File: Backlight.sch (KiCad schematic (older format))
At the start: 26 parts, among them U201 TPS61181, U202 TPS61181

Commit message: Initial footprint association, last few footprints
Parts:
- C201, C202, C203, C204, C207, C208: footprint (none) -> FT:1206
- C205, C206: footprint (none) -> SMD_Packages:SMD-0402_c
- D201, D202: footprint (none) -> novepad:POWERDI123_DIODE
- L201, L202: footprint (none) -> novepad:NR4018_IND
- R201, R202, R203, R204, R205: footprint (none) -> FT:0603
- TP201, TP202, TP203, TP204, TP205, TP206: footprint (none) -> novepad:SMD_TEST_POINT
- U201, U202: footprint (none) -> novepad:QFN50P300X300X80-17N
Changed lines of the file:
@@
 LIBS:valves
 LIBS:novepad-cache
-EELAYER 24 0
+EELAYER 25 0
 EELAYER END
 $Descr A4 11693 8268
@@
 F 0 "R201" V 1430 2200 40  0000 C CNN
 F 1 "0R DNP" V 1357 2201 40  0000 C CNN
-F 2 "" V 1280 2200 30  0000 C CNN
+F 2 "FT:0603" V 1280 2200 30  0001 C CNN
 F 3 "" H 1350 2200 30  0000 C CNN
 	1    1350 2200
@@
 F 0 "TP202" H 1880 1400 40  0000 L CNN
 F 1 "CONN_1" H 1800 1455 30  0001 C CNN
-F 2 "" H 1800 1400 60  0000 C CNN
+F 2 "novepad:SMD_TEST_POINT" H 1800 1400 60  0001 C CNN
 F 3 "" H 1800 1400 60  0000 C CNN
 	1    1800 1400
@@
 F 0 "TP203" H 1880 1550 40  0000 L CNN
 F 1 "CONN_1" H 1800 1605 30  0001 C CNN
-F 2 "" H 1800 1550 60  0000 C CNN
+F 2 "novepad:SMD_TEST_POINT" H 1800 1550 60  0001 C CNN
 F 3 "" H 1800 1550 60  0000 C CNN
 	1    1800 1550
@@
 F 0 "TP201" H 1730 2050 40  0000 L CNN
 F 1 "CONN_1" H 1650 2105 30  0001 C CNN
-F 2 "" H 1650 2050 60  0000 C CNN
+F 2 "novepad:SMD_TEST_POINT" H 1650 2050 60  0001 C CNN
 F 3 "" H 1650 2050 60  0000 C CNN
 	1    1650 2050
@@
 F 0 "TP204" H 2830 1000 40  0000 L CNN
 F 1 "CONN_1" H 2750 1055 30  0001 C CNN
-F 2 "" H 2750 1000 60  0000 C CNN
+F 2 "novepad:SMD_TEST_POINT" H 2750 1000 60  0001 C CNN
 F 3 "" H 2750 1000 60  0000 C CNN
 	1    2750 1000
@@
 F 0 "U202" H 5650 5000 60  0000 C CNN
 F 1 "TPS61181" H 5100 5600 60  0000 C CNN
-F 2 "" H 5550 5600 60  0000 C CNN
+F 2 "novepad:QFN50P300X300X80-17N" H 5550 5600 60  0001 C CNN
 F 3 "" H 5550 5600 60  0000 C CNN
 	1    5100 5550
@@
 F 0 "C203" H 3300 4750 40  0000 L CNN
 F 1 "4.7uF 25V" H 3306 4565 40  0000 L CNN
-F 2 "" H 3338 4500 30  0000 C CNN
+F 2 "FT:1206" H 3338 4500 30  0001 C CNN
 F 3 "" H 3300 4650 60  0000 C CNN
 	1    3300 4650
@@
 F 0 "R203" V 3830 4700 40  0000 C CNN
 F 1 "51R" V 3757 4701 40  0000 C CNN
-F 2 "" V 3680 4700 30  0000 C CNN
+F 2 "FT:0603" V 3680 4700 30  0001 C CNN
 F 3 "" H 3750 4700 30  0000 C CNN
 	1    3750 4700
@@
 F 0 "C204" H 3300 5500 40  0000 L CNN
 F 1 "1uF 25V" H 3306 5315 40  0000 L CNN
-F 2 "" H 3338 5250 30  0000 C CNN
+F 2 "FT:1206" H 3338 5250 30  0001 C CNN
 F 3 "" H 3300 5400 60  0000 C CNN
 	1    3300 5400
@@
 F 0 "C206" H 3650 5900 40  0000 L CNN
 F 1 "100nF" H 3656 5715 40  0000 L CNN
-F 2 "" H 3688 5650 30  0000 C CNN
+F 2 "SMD_Packages:SMD-0402_c" H 3688 5650 30  0001 C CNN
 F 3 "" H 3650 5800 60  0000 C CNN
 	1    3650 5800
@@
 F 0 "R205" V 4080 6300 40  0000 C CNN
 F 1 "68K 1%" V 4007 6301 40  0000 C CNN
-F 2 "" V 3930 6300 30  0000 C CNN
+F 2 "FT:0603" V 3930 6300 30  0001 C CNN
 F 3 "" H 4000 6300 30  0000 C CNN
 	1    4000 6300
@@
 F 0 "L202" H 4800 4550 40  0000 C CNN
 F 1 "10uH NR4018T100M" H 4850 4350 40  0000 C CNN
-F 2 "" H 4900 4450 60  0000 C CNN
+F 2 "novepad:NR4018_IND" H 4900 4450 60  0001 C CNN
 F 3 "" H 4900 4450 60  0000 C CNN
 	1    4900 4450
@@
 F 0 "TP206" H 4630 4750 40  0000 L CNN
 F 1 "CONN_1" H 4550 4805 30  0001 C CNN
-F 2 "" H 4550 4750 60  0000 C CNN
+F 2 "novepad:SMD_TEST_POINT" H 4550 4750 60  0001 C CNN
 F 3 "" H 4550 4750 60  0000 C CNN
 	1    4550 4750
@@
 F 0 "D202" H 5750 4550 40  0000 C CNN
 F 1 "DFLS160-7" H 5750 4350 40  0000 C CNN
-F 2 "" H 5750 4450 60  0000 C CNN
+F 2 "novepad:POWERDI123_DIODE" H 5750 4450 60  0001 C CNN
 F 3 "" H 5750 4450 60  0000 C CNN
 	1    5750 4450
@@
 F 0 "C208" H 6050 4800 40  0000 L CNN
 F 1 "4.7uF 25V" H 6056 4615 40  0000 L CNN
-F 2 "" H 6088 4550 30  0000 C CNN
+F 2 "FT:1206" H 6088 4550 30  0001 C CNN
 F 3 "" H 6050 4700 60  0000 C CNN
 	1    6050 4700
@@
 F 0 "U201" H 5650 2300 60  0000 C CNN
 F 1 "TPS61181" H 5100 2900 60  0000 C CNN
-F 2 "" H 5550 2900 60  0000 C CNN
+F 2 "novepad:QFN50P300X300X80-17N" H 5550 2900 60  0001 C CNN
 F 3 "" H 5550 2900 60  0000 C CNN
 	1    5100 2850
@@
 F 0 "C201" H 3300 2050 40  0000 L CNN
 F 1 "4.7uF 25V" H 3306 1865 40  0000 L CNN
-F 2 "" H 3338 1800 30  0000 C CNN
+F 2 "FT:1206" H 3338 1800 30  0001 C CNN
 F 3 "" H 3300 1950 60  0000 C CNN
 	1    3300 1950
@@
 F 0 "R202" V 3830 2000 40  0000 C CNN
 F 1 "51R" V 3757 2001 40  0000 C CNN
-F 2 "" V 3680 2000 30  0000 C CNN
+F 2 "FT:0603" V 3680 2000 30  0001 C CNN
 F 3 "" H 3750 2000 30  0000 C CNN
 	1    3750 2000
@@
 F 0 "C202" H 3300 2800 40  0000 L CNN
 F 1 "1uF 25V" H 3306 2615 40  0000 L CNN
-F 2 "" H 3338 2550 30  0000 C CNN
+F 2 "FT:1206" H 3338 2550 30  0001 C CNN
 F 3 "" H 3300 2700 60  0000 C CNN
 	1    3300 2700
@@
 F 0 "C205" H 3650 3200 40  0000 L CNN
 F 1 "100nF" H 3656 3015 40  0000 L CNN
-F 2 "" H 3688 2950 30  0000 C CNN
+F 2 "SMD_Packages:SMD-0402_c" H 3688 2950 30  0001 C CNN
 F 3 "" H 3650 3100 60  0000 C CNN
 	1    3650 3100
@@
 F 0 "R204" V 4080 3600 40  0000 C CNN
 F 1 "68K 1%" V 4007 3601 40  0000 C CNN
-F 2 "" V 3930 3600 30  0000 C CNN
+F 2 "FT:0603" V 3930 3600 30  0001 C CNN
 F 3 "" H 4000 3600 30  0000 C CNN
 	1    4000 3600
@@
 F 0 "L201" H 4800 1850 40  0000 C CNN
 F 1 "10uH NR4018T100M" H 4850 1650 40  0000 C CNN
-F 2 "" H 4900 1750 60  0000 C CNN
+F 2 "novepad:NR4018_IND" H 4900 1750 60  0001 C CNN
 F 3 "" H 4900 1750 60  0000 C CNN
 	1    4900 1750
@@
 F 0 "TP205" H 4630 2050 40  0000 L CNN
 F 1 "CONN_1" H 4550 2105 30  0001 C CNN
-F 2 "" H 4550 2050 60  0000 C CNN
+F 2 "novepad:SMD_TEST_POINT" H 4550 2050 60  0001 C CNN
 F 3 "" H 4550 2050 60  0000 C CNN
 	1    4550 2050
@@
 F 0 "D201" H 5750 1850 40  0000 C CNN
 F 1 "DFLS160-7" H 5750 1650 40  0000 C CNN
-F 2 "" H 5750 1750 60  0000 C CNN
+F 2 "novepad:POWERDI123_DIODE" H 5750 1750 60  0001 C CNN
 F 3 "" H 5750 1750 60  0000 C CNN
 	1    5750 1750
@@
 F 0 "C207" H 6050 2100 40  0000 L CNN
 F 1 "4.7uF 25V" H 6056 1915 40  0000 L CNN
-F 2 "" H 6088 1850 30  0000 C CNN
+F 2 "FT:1206" H 6088 1850 30  0001 C CNN
 F 3 "" H 6050 2000 60  0000 C CNN
 	1    6050 2000
@@
 F 0 "TH201" V 1710 890 50  0000 C CNN
 F 1 "NTPA7220LBMB0 1A 22R INRUSH LIMITER" V 1930 1000 50  0000 C CNN
-F 2 "" H 1800 1000 60  0000 C CNN
+F 2 "" H 1800 1000 60  0001 C CNN
 F 3 "" H 1800 1000 60  0000 C CNN
 	1    1800 1000

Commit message: First attempt at routing the high speed differential traces
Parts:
- TH201: footprint (none) -> novepad:PTH_2HOLE_5MM
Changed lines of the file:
@@
 F 0 "TH201" V 1710 890 50  0000 C CNN
 F 1 "NTPA7220LBMB0 1A 22R INRUSH LIMITER" V 1930 1000 50  0000 C CNN
-F 2 "" H 1800 1000 60  0001 C CNN
+F 2 "novepad:PTH_2HOLE_5MM" H 1800 1000 60  0001 C CNN
 F 3 "" H 1800 1000 60  0000 C CNN
 	1    1800 1000

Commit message: Super-zealous length matching version
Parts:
- C205, C206: footprint SMD_Packages:SMD-0402_c -> FT:C0402
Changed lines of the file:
@@
 F 0 "C206" H 3650 5900 40  0000 L CNN
 F 1 "100nF" H 3656 5715 40  0000 L CNN
-F 2 "SMD_Packages:SMD-0402_c" H 3688 5650 30  0001 C CNN
+F 2 "FT:C0402" H 3688 5650 30  0001 C CNN
 F 3 "" H 3650 5800 60  0000 C CNN
 	1    3650 5800
@@
 F 0 "C205" H 3650 3200 40  0000 L CNN
 F 1 "100nF" H 3656 3015 40  0000 L CNN
-F 2 "SMD_Packages:SMD-0402_c" H 3688 2950 30  0001 C CNN
+F 2 "FT:C0402" H 3688 2950 30  0001 C CNN
 F 3 "" H 3650 3100 60  0000 C CNN
 	1    3650 3100

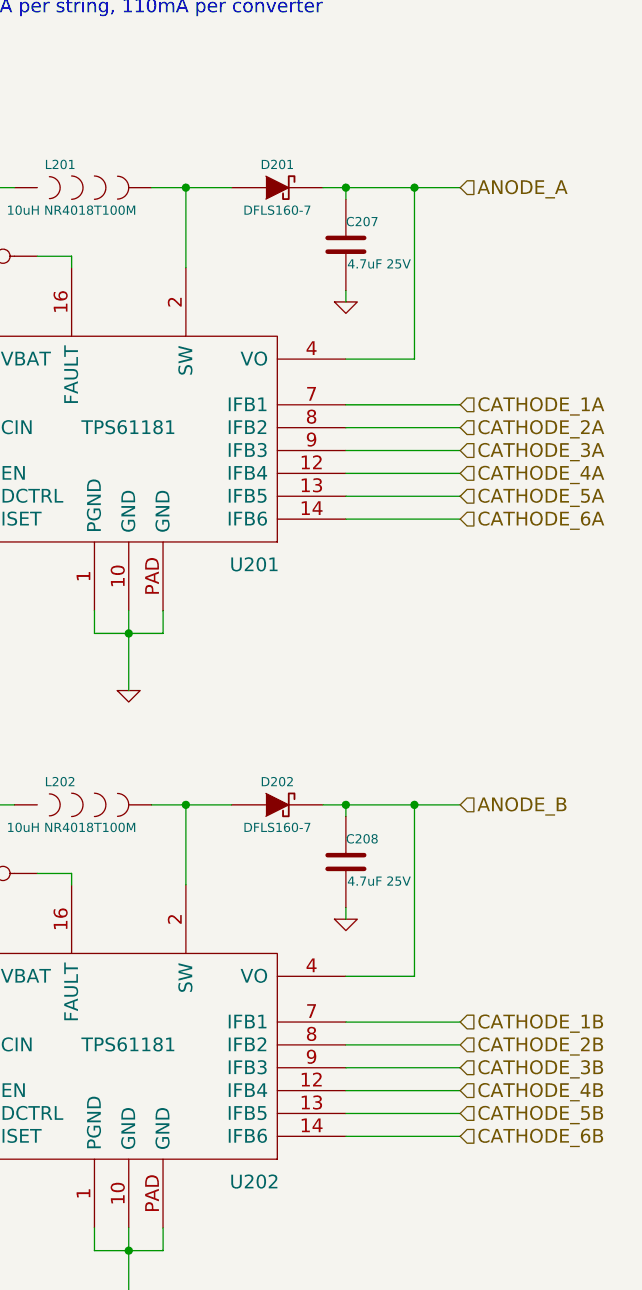
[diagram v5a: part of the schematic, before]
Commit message: Routed, passes DRC
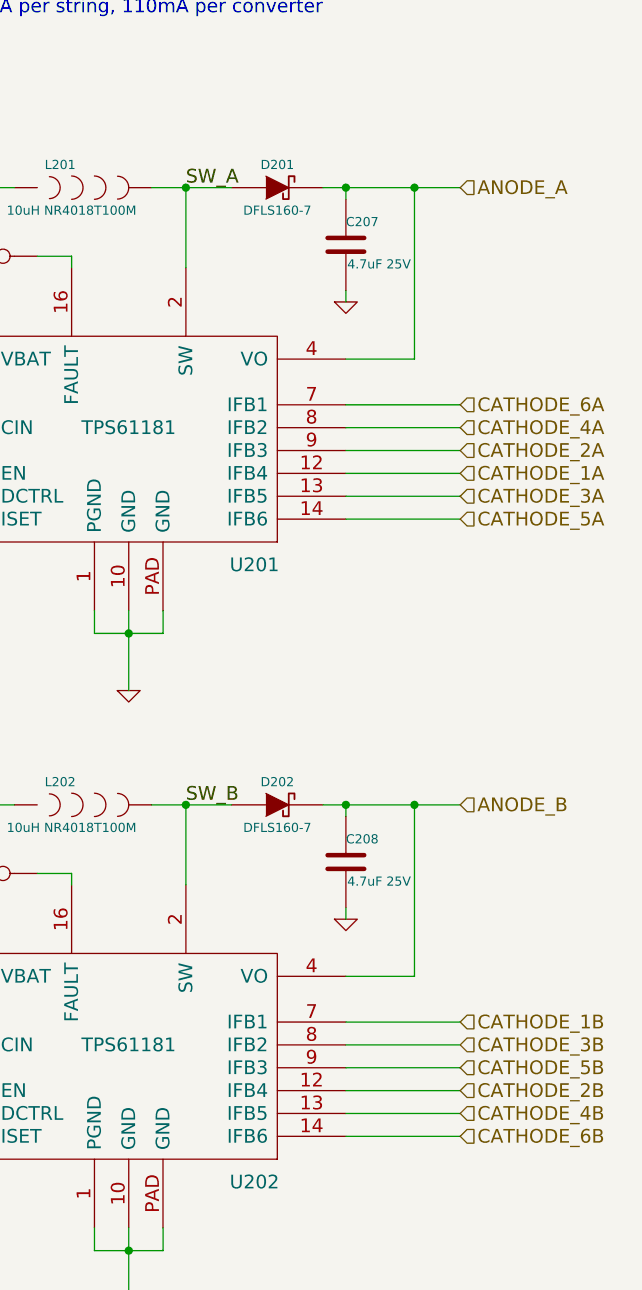
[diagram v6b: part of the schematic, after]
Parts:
- C201, C203, C207, C208: footprint FT:1206 -> FT:0805
- C202, C204: footprint FT:1206 -> FT:0603
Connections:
- net labels added: SW_A, SW_B
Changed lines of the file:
@@
 Text HLabel 6550 1750 2    60   Input ~ 0
 ANODE_A
+Text HLabel 6550 3000 2    60   Input ~ 0
+CATHODE_1A
+Text HLabel 6550 2900 2    60   Input ~ 0
+CATHODE_2A
+Text HLabel 6550 3100 2    60   Input ~ 0
+CATHODE_3A
+Text HLabel 6550 2800 2    60   Input ~ 0
+CATHODE_4A
+Text HLabel 6550 3200 2    60   Input ~ 0
+CATHODE_5A
 Text HLabel 6550 2700 2    60   Input ~ 0
-CATHODE_1A
-Text HLabel 6550 2800 2    60   Input ~ 0
-CATHODE_2A
-Text HLabel 6550 2900 2    60   Input ~ 0
-CATHODE_3A
-Text HLabel 6550 3000 2    60   Input ~ 0
-CATHODE_4A
-Text HLabel 6550 3100 2    60   Input ~ 0
-CATHODE_5A
-Text HLabel 6550 3200 2    60   Input ~ 0
 CATHODE_6A
 Text HLabel 6550 4450 2    60   Input ~ 0
@@
 Text HLabel 6550 5400 2    60   Input ~ 0
 CATHODE_1B
+Text HLabel 6550 5700 2    60   Input ~ 0
+CATHODE_2B
 Text HLabel 6550 5500 2    60   Input ~ 0
-CATHODE_2B
+CATHODE_3B
+Text HLabel 6550 5800 2    60   Input ~ 0
+CATHODE_4B
 Text HLabel 6550 5600 2    60   Input ~ 0
-CATHODE_3B
-Text HLabel 6550 5700 2    60   Input ~ 0
-CATHODE_4B
-Text HLabel 6550 5800 2    60   Input ~ 0
 CATHODE_5B
 Text HLabel 6550 5900 2    60   Input ~ 0
@@
 F 0 "C203" H 3300 4750 40  0000 L CNN
 F 1 "4.7uF 25V" H 3306 4565 40  0000 L CNN
-F 2 "FT:1206" H 3338 4500 30  0001 C CNN
+F 2 "FT:0805" H 3338 4500 30  0001 C CNN
 F 3 "" H 3300 4650 60  0000 C CNN
 	1    3300 4650
@@
 F 0 "C204" H 3300 5500 40  0000 L CNN
 F 1 "1uF 25V" H 3306 5315 40  0000 L CNN
-F 2 "FT:1206" H 3338 5250 30  0001 C CNN
+F 2 "FT:0603" H 3338 5250 30  0001 C CNN
 F 3 "" H 3300 5400 60  0000 C CNN
 	1    3300 5400
@@
 F 0 "C208" H 6050 4800 40  0000 L CNN
 F 1 "4.7uF 25V" H 6056 4615 40  0000 L CNN
-F 2 "FT:1206" H 6088 4550 30  0001 C CNN
+F 2 "FT:0805" H 6088 4550 30  0001 C CNN
 F 3 "" H 6050 4700 60  0000 C CNN
 	1    6050 4700
@@
 F 0 "C201" H 3300 2050 40  0000 L CNN
 F 1 "4.7uF 25V" H 3306 1865 40  0000 L CNN
-F 2 "FT:1206" H 3338 1800 30  0001 C CNN
+F 2 "FT:0805" H 3338 1800 30  0001 C CNN
 F 3 "" H 3300 1950 60  0000 C CNN
 	1    3300 1950
@@
 F 0 "C202" H 3300 2800 40  0000 L CNN
 F 1 "1uF 25V" H 3306 2615 40  0000 L CNN
-F 2 "FT:1206" H 3338 2550 30  0001 C CNN
+F 2 "FT:0603" H 3338 2550 30  0001 C CNN
 F 3 "" H 3300 2700 60  0000 C CNN
 	1    3300 2700
@@
 F 0 "C207" H 6050 2100 40  0000 L CNN
 F 1 "4.7uF 25V" H 6056 1915 40  0000 L CNN
-F 2 "FT:1206" H 6088 1850 30  0001 C CNN
+F 2 "FT:0805" H 6088 1850 30  0001 C CNN
 F 3 "" H 6050 2000 60  0000 C CNN
 	1    6050 2000
@@
 Wire Wire Line
 	1550 1000 1350 1000
+Text Label 5350 1750 0    60   ~ 0
+SW_A
+Text Label 5350 4450 0    60   ~ 0
+SW_B
 $EndSCHEMATC
